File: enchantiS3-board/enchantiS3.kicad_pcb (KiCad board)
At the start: 4 copper layers, 55.9 x 25.4 mm, 66 parts, among them J1 USB_C_Receptacle_USB2.0, Q1 BSS138, Q2 BSS138, Q3 BSS138, SW1 B3U-1000P, SW2 B3U-1000P, U1 USBLC6-2P6, U2 MCP73871, U3 NCP167AMX330TBG, U4 NCP167AMX180TBG

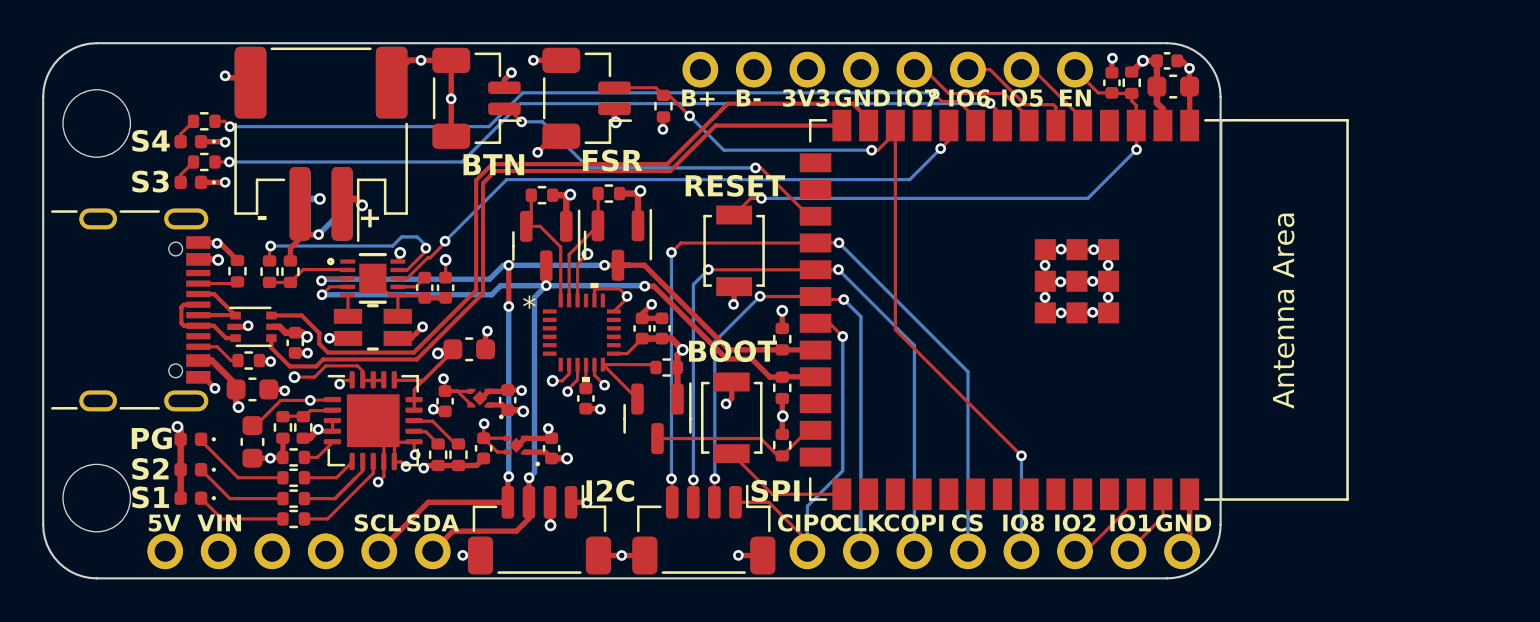
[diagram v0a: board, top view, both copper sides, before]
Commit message: added revision 3 board design
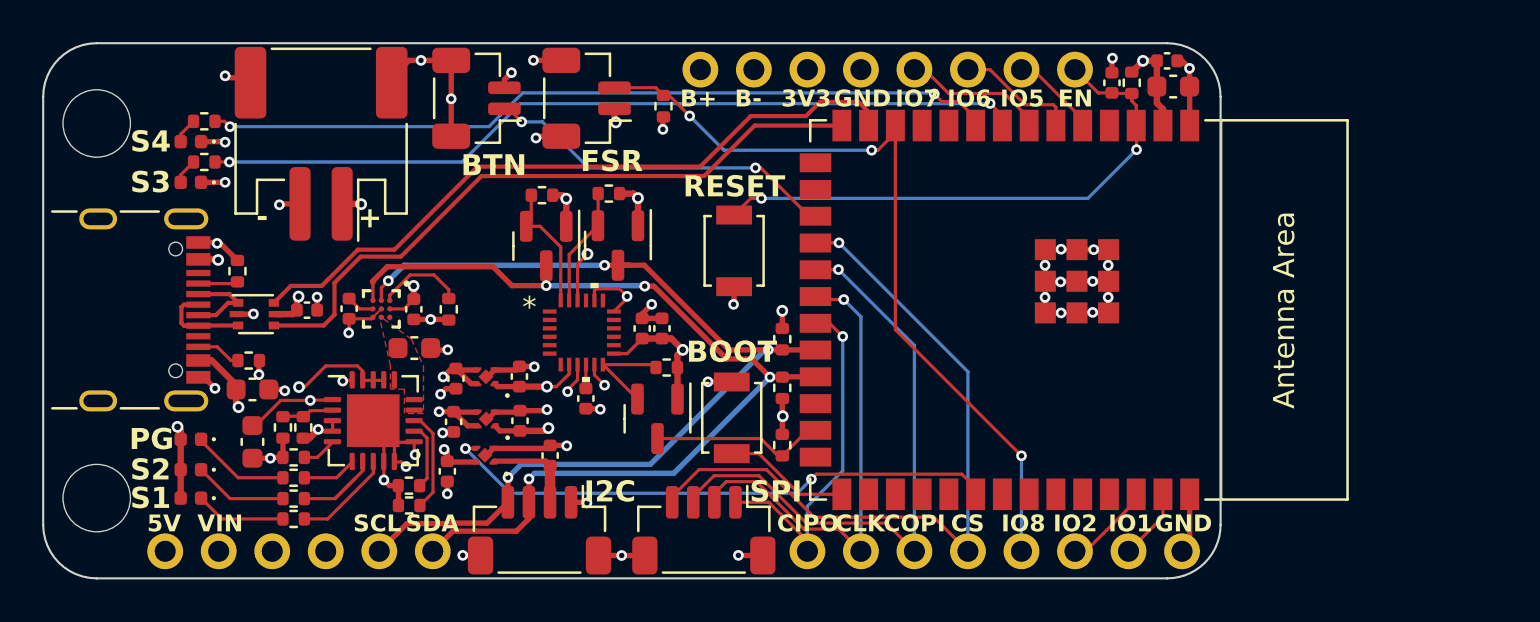
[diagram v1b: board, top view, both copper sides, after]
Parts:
- removed BT2: JST-PH-1x02-2.000mm, Connector_JST:JST_PH_S2B-PH-SM4-TB_1x02-1MP_P2.00mm_Horizontal
- removed FG1: MAX17055ETB+T, max17055-footprints:21-100013A_T102A2&plus_1C_MXM
- removed R12: 10k, Resistor_SMD:R_0402_1005Metric
- removed R2: Ohmite_LVK12 10m, ul_LVK12R010CER-footprints:LVK12_OHM-L
- added C16: 1uF, Capacitor_SMD:C_0402_1005Metric, F.Cu at (116.8, 67.8)
- added C17: 1uF, Capacitor_SMD:C_0402_1005Metric, F.Cu at (111.9, 68.6)
- added U5: NCP167AMX330TBG, NCP167AMX330TBG-footprints:XDFN4_1X1_711AJ_ONS, F.Cu at (113.7, 67.8)
- added U6: MAX17262REWL+T, max17262-footprints:21-100221A_W91G1&plus_3_MXM, F.Cu at (108.8, 60.9)
- moved TH1 7.72 mm to (112.0, 60.9), turned to -90 degrees
- moved C2 3.72 mm to (107.2, 60.9)
- moved R20 3.36 mm to (110.1, 70.2), turned to 0 degrees
- moved C8 2.60 mm to (110.3, 62.7)
- moved R17 2.02 mm to (110.1, 69.3), turned to 0 degrees
- moved C5 1.99 mm to (115.3, 66.2)
- moved C4 1.90 mm to (112.2, 66.2)
- moved U3 1.90 mm to (113.7, 66.1)
- moved C1 1.82 mm to (110.3, 60.9)
- moved C15 1.65 mm to (105.2, 60.9), turned to 0 degrees
- moved C12 1.25 mm to (115.3, 64.1)
- moved C11 1.19 mm to (112.3, 64.2)
- moved U4 1.05 mm to (113.7, 64.1)
- moved U1 0.61 mm to (102.8, 61.1)
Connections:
- BOARDLAYOUT1 pad 1.2: -BATT -> GND
- BT1 pad 2: -BATT -> GND
- C1 pad 2: CSP -> GND
- C2 pad 2: CSP -> GND
- C8 pad 1: +BATT -> CHRG+
- TH1 pad 1: /AIN -> /THRM
- TH1 pad 2: -BATT -> GND
- TOUCH1 pad 2: +3V3 -> 3V3_AUX
- U2 pad 14: +BATT -> CHRG+
- U2 pad 15: +BATT -> CHRG+
- U2 pad 16: +BATT -> CHRG+
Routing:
- net -BATT: track 37.9 -> 0.00 mm, vias 2 -> 0
- net /IO17: track 29.6 -> 0.00 mm, vias 2 -> 0
- net /IO39: track 0.00 -> 26.6 mm, vias 0 -> 2
- net +BATT: track 11.4 -> 2.87 mm, vias 5 -> 2
- net /THRM: track 10.3 -> 4.25 mm, vias 2 -> 0
- net /USBD-: track 37.9 -> 33.0 mm
- net GND: track 80.4 -> 85.3 mm, vias 48 -> 52
- net CSP: track 4.84 -> 0.00 mm
- net 3V3_AUX: track 0.00 -> 4.78 mm
- net /SCLK: track 27.0 -> 22.7 mm, vias 3 -> 1
- net /AIN: track 4.02 -> 0.00 mm
- net /USBD+: track 35.7 -> 31.8 mm
- net /COPI: track 32.4 -> 28.6 mm, vias 3 -> 1
- net /CS: track 37.2 -> 34.7 mm, vias 3 -> 1
- net /PROG1: track 2.55 -> 4.83 mm
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- added copper zone on F.Cu, net CHRG+
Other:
- board text added: "EnchantiS3 v0.3 2024-02 IDMIL McGill University Albert Niyonsenga"
- board text removed: "BAT"
- board text removed: "EnchantiS3 v0.1 2023-12 IDMIL McGill University Albert Niyonsenga"

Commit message: switched IMU to LSM6DS16X, changed board to 2 layer, updated passives to 0603 size
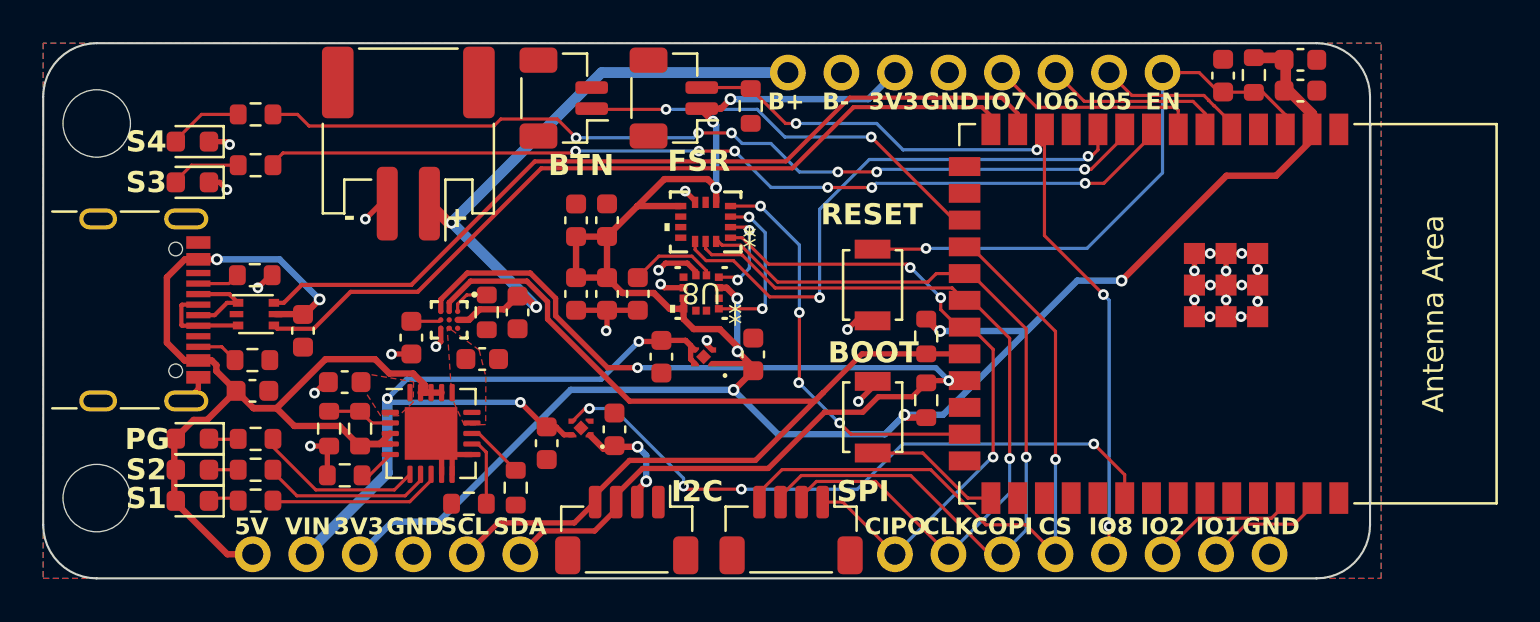
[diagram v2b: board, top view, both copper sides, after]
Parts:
- removed C11, C12: 1uF, Capacitor_SMD:C_0402_1005Metric
- removed IMU1: ICM-20948, ICM20948-footprints:QFN24_3X3X0P9_IVS
- removed Q1, Q2, Q3: BSS138, Package_TO_SOT_SMD:SOT-23
- removed R14, R15, R16, R19, R21, R23: 2k2, Resistor_SMD:R_0402_1005Metric
- removed U4: NCP167AMX180TBG, NCP167AMX330TBG-footprints:XDFN4_1X1_711AJ_ONS
- added C18: 0.1uF, Capacitor_SMD:C_0603_1608Metric, F.Cu at (119.5, 60.2)
- added C20: 0.1uF, Capacitor_SMD:C_0603_1608Metric, F.Cu at (119.5, 56.7)
- added R11: 2k2, Resistor_SMD:R_0603_1608Metric, F.Cu at (134.6, 62.2)
- added R2: 2k2, Resistor_SMD:R_0603_1608Metric, F.Cu at (134.6, 65.2)
- added U7: LSM6DSV16XTR, LSM6DSV16XTR-footprints:LGA14L_LSM6_STM, F.Cu at (124.2, 56.7)
- added U8: IIS2MDCTR, IIS2MDCTR-footprints:LGA-12_2X2X0P7_STM, F.Cu at (123.9, 60.1)
- C1, C10, C15, C16, C17, C19, C2, C4, C5, C9: footprint Capacitor_SMD:C_0402_1005Metric -> Capacitor_SMD:C_0603_1608Metric
- C6: value 0.1uF -> 220nF; footprint Capacitor_SMD:C_0402_1005Metric -> Capacitor_SMD:C_0603_1608Metric
- C7: value 0.1uF -> 1uF; footprint Capacitor_SMD:C_0402_1005Metric -> Capacitor_SMD:C_0603_1608Metric
- CHARGLED1, CHARGLED2, CHARGLED3, STATLED1, STATLED2: footprint LED_SMD:LED_0402_1005Metric -> LED_SMD:LED_0603_1608Metric
- R1, R10, R17, R18, R22, R24, R3, R4, R5, R6, R7, R8, R9, TH1: footprint Resistor_SMD:R_0402_1005Metric -> Resistor_SMD:R_0603_1608Metric
- R20: value 2k -> 1k; footprint Resistor_SMD:R_0402_1005Metric -> Resistor_SMD:R_0603_1608Metric
- moved C5 11.5 mm to (126.4, 63.0)
- moved U3 10.7 mm to (124.1, 63.1)
- moved C4 10.3 mm to (122.0, 63.1)
- moved MCU1 7.08 mm to (145.9, 61.1)
- moved SW2 6.77 mm to (132.1, 59.7)
- moved SW1 6.69 mm to (132.1, 66.0)
- moved C10 6.56 mm to (118.0, 56.7)
- moved C19 6.33 mm to (152.4, 49.0)
- moved C13 6.04 mm to (152.4, 50.5)
- moved R5 5.81 mm to (150.2, 49.8)
- moved C6 5.54 mm to (120.9, 60.2)
- moved C9 5.29 mm to (148.7, 49.8)
- moved C3 5.22 mm to (107.0, 64.3), turned to 180 degrees
- moved R20 5.13 mm to (115.1, 69.4), turned to 90 degrees
- moved C1 4.93 mm to (115.2, 61.0)
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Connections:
- net /IO18 renamed /MAG_INT
- C10 pad 1: +1V8 -> +3V3
- C7 pad 1: +1V8 -> +3V3
- MCU1 pad 10: /IO17 -> /CS1
- MCU1 pad 25: /IO48 -> /IMU_INT
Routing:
- net +3V3: track 10.5 -> 114.2 mm, vias 5 -> 9
- net GND: track 85.3 -> 45.8 mm, vias 52 -> 27
- net VUSB: track 21.2 -> 50.7 mm, vias 6 -> 2
- net +BATT: track 2.87 -> 30.4 mm
- net /CS1: track 0.00 -> 26.8 mm, vias 0 -> 2
- net SYS: track 12.8 -> 35.7 mm, vias 5 -> 3
- net +1V8: track 17.2 -> 0.00 mm, vias 5 -> 0
- net /IMU_INT: track 4.89 -> 19.5 mm, vias 0 -> 4
- net /SCLK: track 22.7 -> 37.0 mm
- net /CIPO: track 17.1 -> 31.1 mm, vias 1 -> 3
- net /COPI: track 28.6 -> 40.7 mm
- net /IO48: track 8.34 -> 0.00 mm
- net /SCL_EXT: track 0.00 -> 7.70 mm, vias 0 -> 2
- net /USBD+: track 31.8 -> 39.3 mm
- net /USBD-: track 33.0 -> 40.4 mm
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- added copper zone on B.Cu, net GND
- added copper zone on F.Cu, net GND
- added copper zone on F.Cu, net SYS
- removed copper zone on In2.Cu, net +1V8
- removed copper zone on In2.Cu, net +3V3
- removed copper zone on In2.Cu, net +BATT
- removed copper zone on In1.Cu, net GND
- removed copper zone on In2.Cu, net SYS
- removed copper zone on In2.Cu, net VUSB
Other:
- board size 55.9 x 25.4 mm -> 63 x 25.4 mm
- copper layers 4 -> 2

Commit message: Revert "switched IMU to LSM6DS16X, changed board to 2 layer, updated passives to 0603 size"
This reverts commit 721c303317f50970347c44c42bf72dd13544c695.
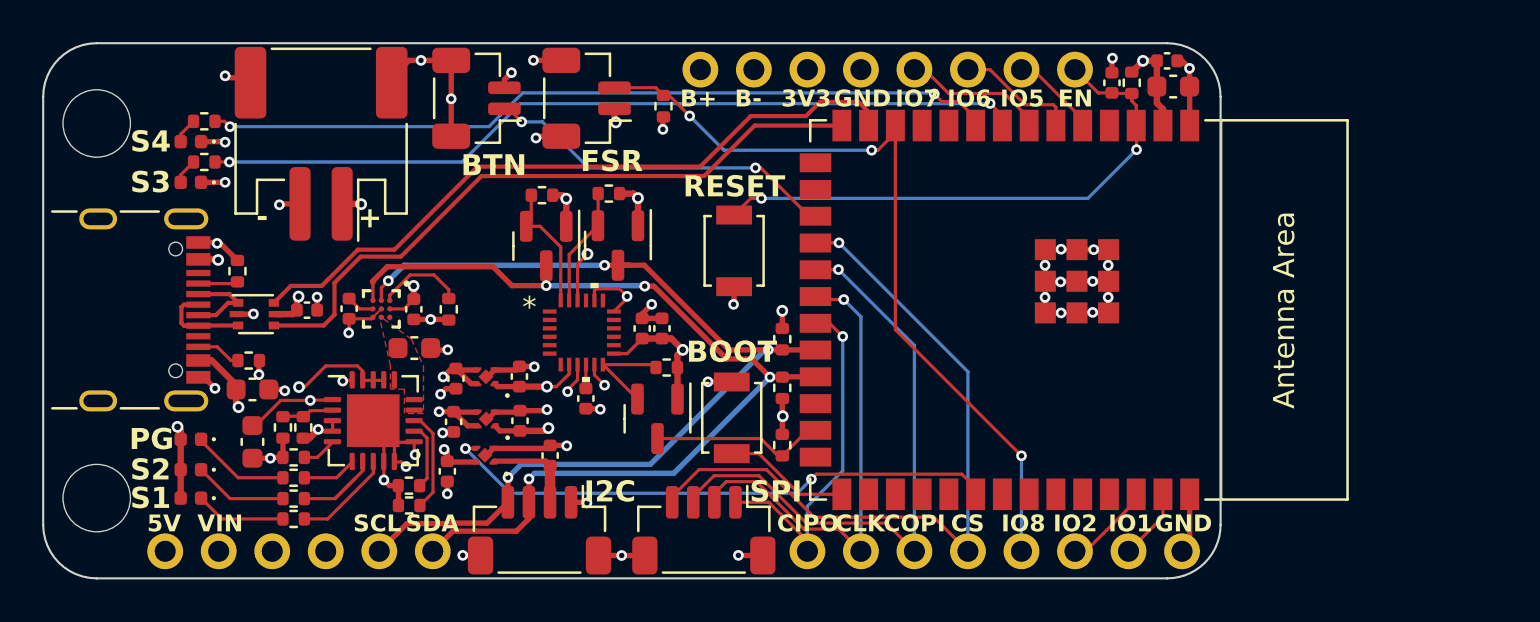
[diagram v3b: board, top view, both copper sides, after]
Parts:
- removed C18, C20: 0.1uF, Capacitor_SMD:C_0603_1608Metric
- removed R11, R2: 2k2, Resistor_SMD:R_0603_1608Metric
- removed U7: LSM6DSV16XTR, LSM6DSV16XTR-footprints:LGA14L_LSM6_STM
- removed U8: IIS2MDCTR, IIS2MDCTR-footprints:LGA-12_2X2X0P7_STM
- added C11: 1uF, Capacitor_SMD:C_0402_1005Metric, F.Cu at (112.3, 64.2)
- added C12: 1uF, Capacitor_SMD:C_0402_1005Metric, F.Cu at (115.3, 64.1)
- added IMU1: ICM-20948, ICM20948-footprints:QFN24_3X3X0P9_IVS, F.Cu at (118.3, 62.0)
- added Q1: BSS138, Package_TO_SOT_SMD:SOT-23, F.Cu at (120.0, 57.9)
- added Q2: BSS138, Package_TO_SOT_SMD:SOT-23, F.Cu at (116.6, 57.9)
- added Q3: BSS138, Package_TO_SOT_SMD:SOT-23, F.Cu at (121.9, 66.1)
- added R14: 2k2, Resistor_SMD:R_0402_1005Metric, F.Cu at (119.6, 55.4)
- added R15: 2k2, Resistor_SMD:R_0402_1005Metric, F.Cu at (116.4, 55.5)
- added R16: 2k2, Resistor_SMD:R_0402_1005Metric, F.Cu at (127.8, 64.6)
- added R19: 2k2, Resistor_SMD:R_0402_1005Metric, F.Cu at (127.8, 62.3)
- added R21: 2k2, Resistor_SMD:R_0402_1005Metric, F.Cu at (122.3, 63.7)
- added R23: 2k2, Resistor_SMD:R_0402_1005Metric, F.Cu at (127.8, 67.3)
- added U4: NCP167AMX180TBG, NCP167AMX330TBG-footprints:XDFN4_1X1_711AJ_ONS, F.Cu at (113.7, 64.1)
- C1, C10, C15, C16, C17, C19, C2, C4, C5, C9: footprint Capacitor_SMD:C_0603_1608Metric -> Capacitor_SMD:C_0402_1005Metric
- C6: value 220nF -> 0.1uF; footprint Capacitor_SMD:C_0603_1608Metric -> Capacitor_SMD:C_0402_1005Metric
- C7: value 1uF -> 0.1uF; footprint Capacitor_SMD:C_0603_1608Metric -> Capacitor_SMD:C_0402_1005Metric
- CHARGLED1, CHARGLED2, CHARGLED3, STATLED1, STATLED2: footprint LED_SMD:LED_0603_1608Metric -> LED_SMD:LED_0402_1005Metric
- R1, R10, R17, R18, R22, R24, R3, R4, R5, R6, R7, R8, R9, TH1: footprint Resistor_SMD:R_0603_1608Metric -> Resistor_SMD:R_0402_1005Metric
- R20: value 1k -> 2k; footprint Resistor_SMD:R_0603_1608Metric -> Resistor_SMD:R_0402_1005Metric
- moved C5 11.5 mm to (115.3, 66.2)
- moved U3 10.7 mm to (113.7, 66.1)
- moved C4 10.3 mm to (112.2, 66.2)
- moved MCU1 7.08 mm to (138.9, 60.9)
- moved SW2 6.77 mm to (125.5, 58.1)
- moved SW1 6.69 mm to (125.4, 66.0)
- moved C10 6.56 mm to (122.1, 61.8)
- moved C19 6.33 mm to (146.1, 49.1)
- moved C13 6.04 mm to (146.3, 50.3)
- moved R5 5.81 mm to (144.4, 50.1)
- moved C6 5.54 mm to (118.5, 65.1)
- moved C9 5.29 mm to (143.4, 50.1)
- moved C3 5.22 mm to (102.6, 67.2), turned to -90 degrees
- moved R20 5.13 mm to (110.1, 70.2), turned to 0 degrees
- moved C1 4.93 mm to (110.3, 60.9)
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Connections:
- net /MAG_INT renamed /IO18
- C10 pad 1: +3V3 -> +1V8
- C7 pad 1: +3V3 -> +1V8
- MCU1 pad 10: /CS1 -> /IO17
- MCU1 pad 25: /IMU_INT -> /IO48
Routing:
- net +3V3: track 114.2 -> 10.5 mm, vias 9 -> 5
- net GND: track 45.8 -> 85.3 mm, vias 27 -> 52
- net VUSB: track 50.7 -> 21.2 mm, vias 2 -> 6
- net +BATT: track 30.4 -> 2.87 mm
- net /CS1: track 26.8 -> 0.00 mm, vias 2 -> 0
- net SYS: track 35.7 -> 12.8 mm, vias 3 -> 5
- net +1V8: track 0.00 -> 17.2 mm, vias 0 -> 5
- net /IMU_INT: track 19.5 -> 4.89 mm, vias 4 -> 0
- net /SCLK: track 37.0 -> 22.7 mm
- net /CIPO: track 31.1 -> 17.1 mm, vias 3 -> 1
- net /COPI: track 40.7 -> 28.6 mm
- net /IO48: track 0.00 -> 8.34 mm
- net /SCL_EXT: track 7.70 -> 0.00 mm, vias 2 -> 0
- net /USBD+: track 39.3 -> 31.8 mm
- net /USBD-: track 40.4 -> 33.0 mm
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- added copper zone on In2.Cu, net +1V8
- added copper zone on In2.Cu, net +3V3
- added copper zone on In2.Cu, net +BATT
- added copper zone on In1.Cu, net GND
- added copper zone on In2.Cu, net SYS
- added copper zone on In2.Cu, net VUSB
- removed copper zone on B.Cu, net GND
- removed copper zone on F.Cu, net GND
- removed copper zone on F.Cu, net SYS
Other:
- board size 63 x 25.4 mm -> 55.9 x 25.4 mm
- copper layers 2 -> 4

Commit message: switched IMU, made USB data traces thicker
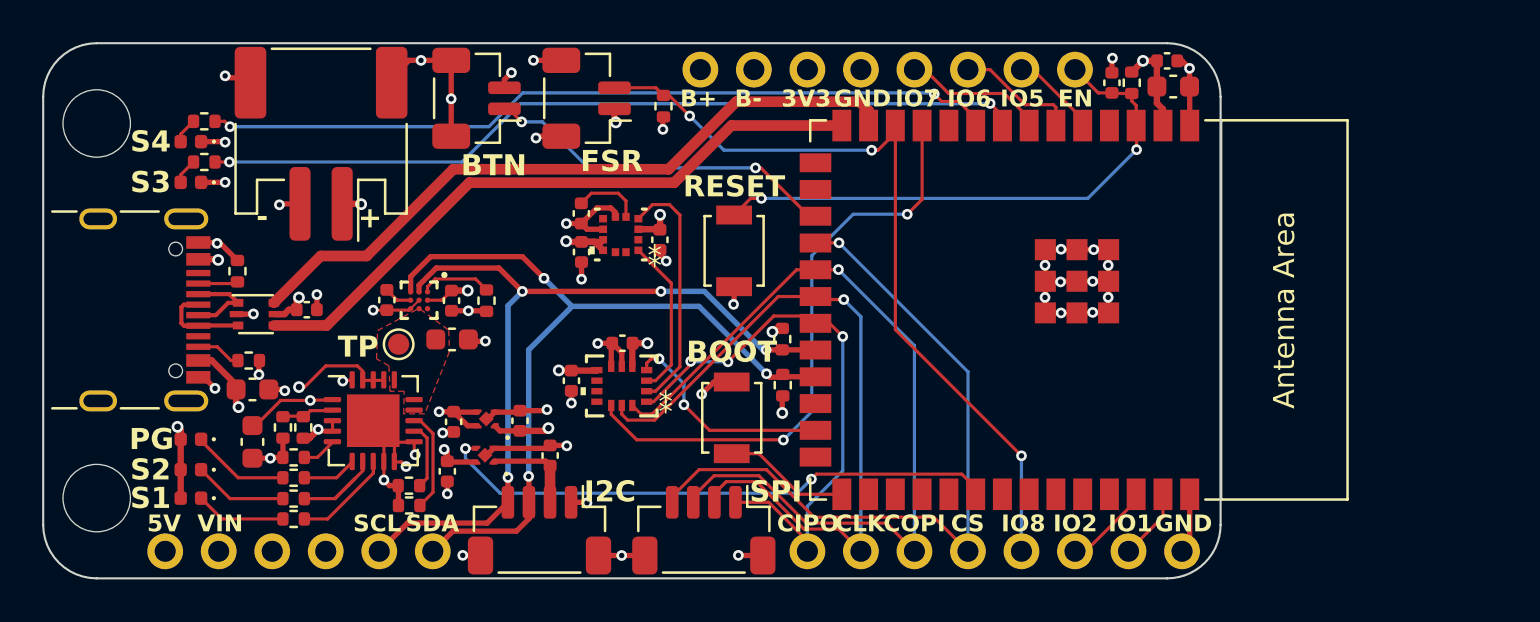
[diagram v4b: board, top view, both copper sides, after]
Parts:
- removed C11, C12: 1uF, Capacitor_SMD:C_0402_1005Metric
- removed IMU1: ICM-20948, ICM20948-footprints:QFN24_3X3X0P9_IVS
- removed Q1, Q2, Q3: BSS138, Package_TO_SOT_SMD:SOT-23
- removed R14, R15, R16, R19, R21, R23: 2k2, Resistor_SMD:R_0402_1005Metric
- removed U4: NCP167AMX180TBG, NCP167AMX330TBG-footprints:XDFN4_1X1_711AJ_ONS
- added C18: 220nF, Capacitor_SMD:C_0402_1005Metric, F.Cu at (118.2, 56.3)
- added C20: 0.1uF, Capacitor_SMD:C_0402_1005Metric, F.Cu at (122.0, 57.6)
- added R12: 2k2, Resistor_SMD:R_0402_1005Metric, F.Cu at (127.8, 64.5)
- added R13: 2k2, Resistor_SMD:R_0402_1005Metric, F.Cu at (127.8, 62.3)
- added TP1: TestPoint, TestPoint:TestPoint_Pad_D1.0mm, F.Cu at (109.6, 62.5)
- added U7: LSM6DSV16XTR, LSM6DSV16XTR-footprints:LGA14L_LSM6_STM, F.Cu at (120.2, 64.5)
- added U8: IIS2MDCTR, IIS2MDCTR-footprints:LGA-12_2X2X0P7_STM, F.Cu at (120.1, 57.3)
- C6: value 0.1uF -> 1uF
- moved C6 6.96 mm to (118.3, 58.2)
- moved C7 4.18 mm to (117.8, 64.3), turned to -90 degrees
- moved C10 2.00 mm to (120.2, 62.5), turned to 180 degrees
- moved C1 1.84 mm to (112.1, 60.5)
- moved TH1 1.84 mm to (113.8, 60.5)
- moved C2 1.84 mm to (109.0, 60.5)
- moved C8 1.84 mm to (112.1, 62.3)
- moved U6 1.84 mm to (110.5, 60.5)
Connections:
- C10 pad 1: +1V8 -> +3V3
- C6 pad 1: Net-(IMU1-REGOUT) -> +3V3
- C7 pad 1: +1V8 -> +3V3
- MCU1 pad 11: /IO18 -> /CS1
- MCU1 pad 25: /IO48 -> /IMU_INT
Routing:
- net /CS1: track 0.00 -> 28.3 mm, vias 0 -> 2
- net +1V8: track 17.2 -> 0.00 mm, vias 5 -> 0
- net /SCLK: track 22.7 -> 34.8 mm
- net /SDA_EXT: track 0.00 -> 11.7 mm
- net /COPI: track 28.6 -> 40.3 mm
- net /CIPO: track 17.1 -> 27.1 mm, vias 1 -> 3
- net /SCL: track 46.9 -> 38.4 mm
- net /IO48: track 8.34 -> 0.00 mm
- net /SCL_EXT: track 0.00 -> 7.56 mm
- net +3V3: track 10.5 -> 17.6 mm, vias 5 -> 9
- net /SDA: track 45.9 -> 38.8 mm, vias 4 -> 3
- net /LV_SDA: track 6.16 -> 0.00 mm
- net /LV_SCL: track 5.64 -> 0.00 mm
- net /IMU_INT: track 4.89 -> 10.4 mm, vias 0 -> 2
- net Net-(U8-C1): track 0.00 -> 3.22 mm
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- removed copper zone on In2.Cu, net +1V8
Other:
- board text added: "TP"
